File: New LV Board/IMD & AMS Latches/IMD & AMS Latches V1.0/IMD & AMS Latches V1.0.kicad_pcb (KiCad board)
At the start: 2 copper layers, 46 x 51.3 mm, 23 parts, among them J2 B12B-PH-K-S, K1 A161CS12VDC.64, K2 A161CS12VDC.64, K3 A161CS12VDC.64, K4 A161CS12VDC.64, K5 A161CS12VDC.64, K6 A161CS12VDC.64, P1 PH1-20-UA, P2 PH1-20-UA, SW1 Test Reset IMD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

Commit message: Added version numbers
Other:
- board text added: "AMS & IMD Latches V1.0 | J.W. Nov 2025"
- board text removed: "AMS & IMD Latches | J.W. Nov 2025"
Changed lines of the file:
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@@
 		)
 	)
-	(gr_text "AMS & IMD Latches | J.W. Nov 2025"
-		(at 67.07892 39.722899 0)
+	(gr_text "AMS & IMD Latches V1.0 | J.W. Nov 2025"
+		(at 65.578919 39.722899 0)
 		(layer "F.SilkS")
 		(effects

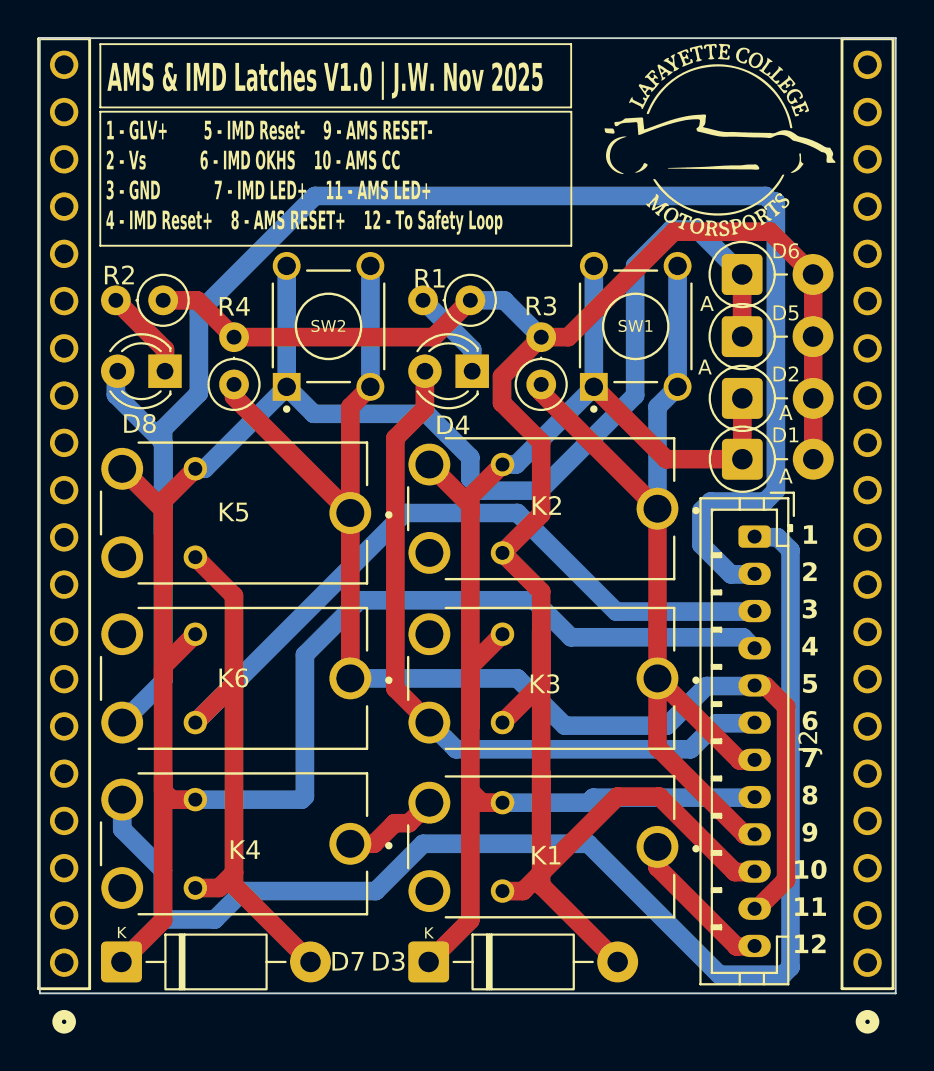
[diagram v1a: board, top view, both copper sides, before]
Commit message: added 3d models to the full part
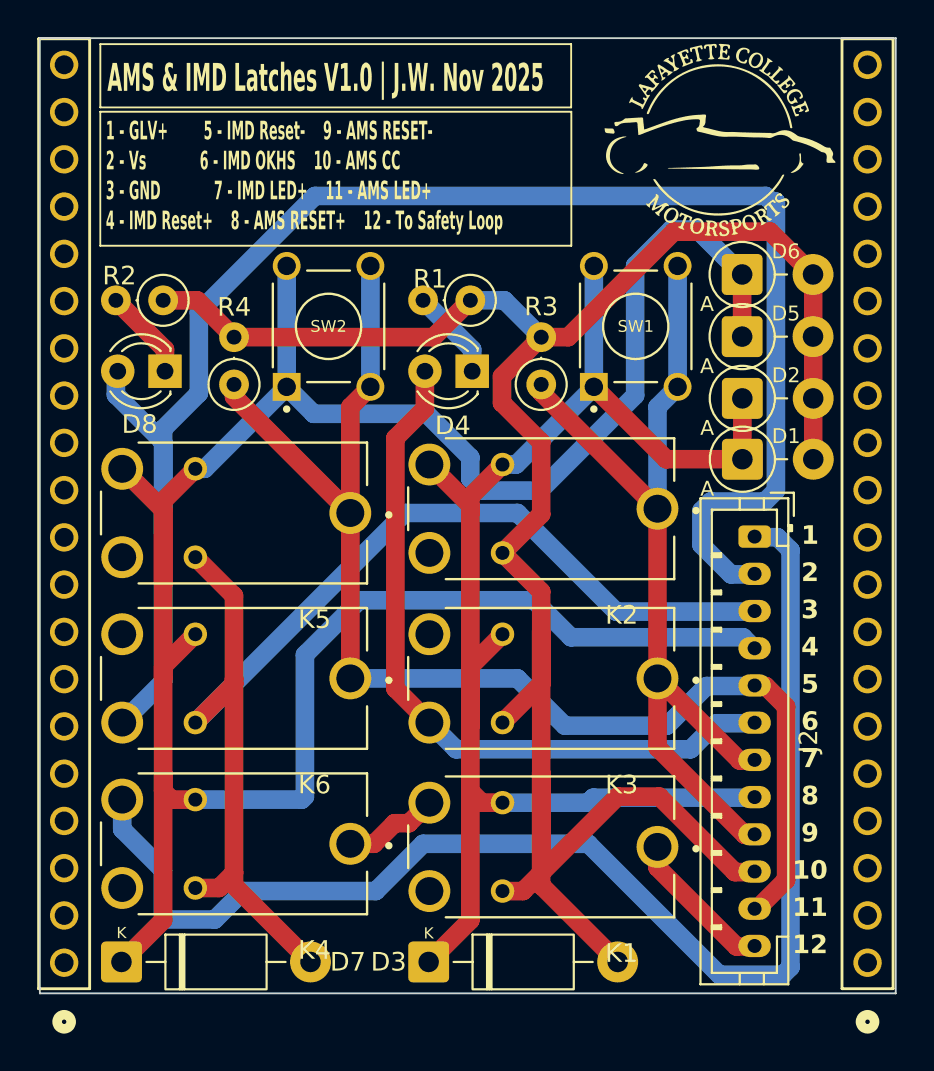
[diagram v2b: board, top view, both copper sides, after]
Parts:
- D1, D2, D5, D6: footprint Diode_THT:D_DO-41_SOD81_P3.81mm_Vertical_AnodeUp -> motorsports:D_DO-41_SOD81_P3.81mm_Vertical_AnodeUp
- K1, K2, K3, K4, K5, K6: footprint Library:RELAY_A161CS12VDC.64 -> motorsports:RELAY_A161CS12VDC.64

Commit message: changes that can probably be overriden?
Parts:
- P1, P2: footprint PH1-20-UA:CONN_PH1-20-UA_ADM -> Connector_PinHeader_2.54mm:PinHeader_1x20_P2.54mm_Vertical
- turned P1 to 180 degrees
- turned P2 to 180 degrees

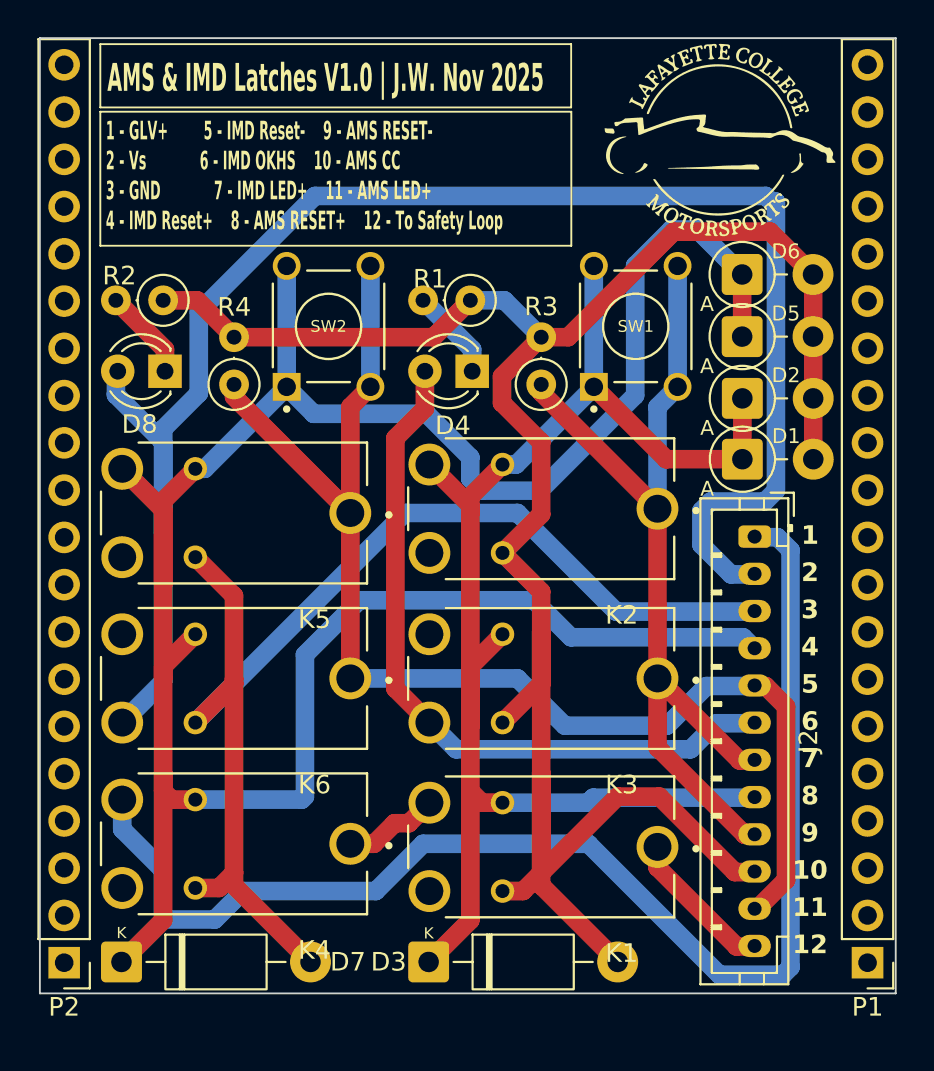
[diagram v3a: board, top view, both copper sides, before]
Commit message: Revert "changes that can probably be overriden?"
This reverts commit 98343f344ad0564068fa41cd25b8ec5d82cca4ea.
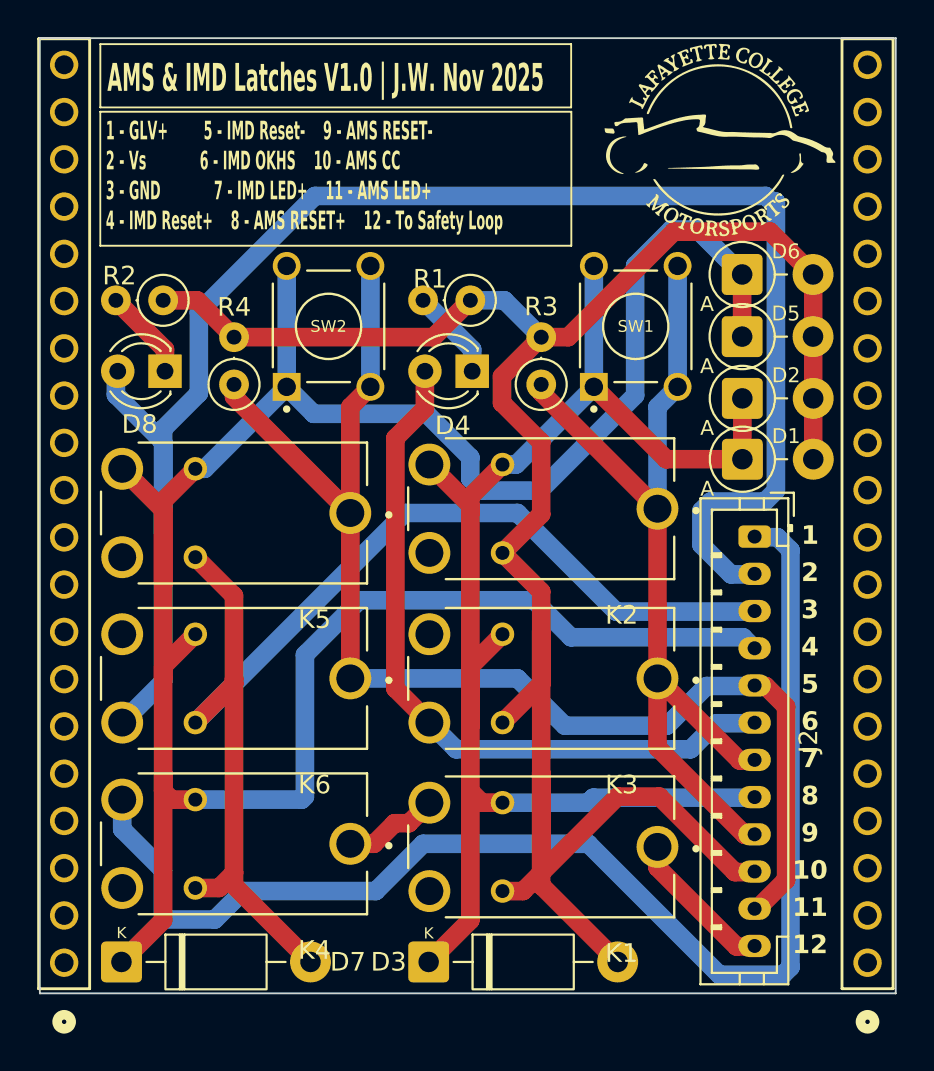
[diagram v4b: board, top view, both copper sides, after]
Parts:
- P1, P2: footprint Connector_PinHeader_2.54mm:PinHeader_1x20_P2.54mm_Vertical -> PH1-20-UA:CONN_PH1-20-UA_ADM
- turned P1 to 90 degrees
- turned P2 to 90 degrees
